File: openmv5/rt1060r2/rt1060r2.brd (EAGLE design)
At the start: 35.6 x 44.5 mm, 239 parts, among them CN1 S2B-PH-K-S(LF)(SN), IC1 LM66200DRLR, IC10 TCR2LF33,LM_CT, IC2 AP61300Z6-7, IC3 IS42S16160G-6BL, IC4 ATECC608B-MAHDA-T, IC5 IS25LP064D-JKLE-TR, IC7 MXC4005XC, IC8 MIMXRT1052DVL6B, IC9 KSZ8081RNDCA-TR, J1 USB4105-GF-A, J2 DNP, J3 DNP, J4 DF12-36-DS, J5 USD-1040310811, J6 DNP, J7 DNP, J8 3221-10-0300-00, M1 9774030151R, M2 9774030151R, Q1 2N7002KW_R1_00001, Q2 2N7002KW_R1_00001, Q3 2N7002KW_R1_00001, Q4 2N7002KW_R1_00001, Q5 2N7002KW_R1_00001, Q6 DMG2301L-7, Q7 2N7002KW_R1_00001, U2 BQ24075RGTR, U3 LBEE5KL1DX-883, Y1 SC32S-7PF20PPM, Y2 XRCGB24M000F3M00R0, Y3 ECS-327MVATX-3-CN-TR3

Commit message: Update R2 board per all feedback so far
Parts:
- removed C111: 0.1uF, 0402:0402
- removed IC10: TCR2LF33,LM_CT, TCR2LF33_LM_CT:TCR2LF33LMCT
- removed L9: MAKK2016T2R2M, MAKK2016T2R2M:INDC2016X100N
- removed U3: LBEE5KL1DX-883, LBEE5KL1DX-TEMP:XCVR_LBEE5KL1DX-TEMP
- added C24: 0.22uF, rcl:C0201
- added C25: 4.7uF, 0402:0402
- added D11, D12, D13, D14: CPDQT5V0HE-HF, CPDQT5V0HE-HF:CPDQT5V0HEHF
- added D15: RB521S30T5G, RB521S30T5G:SODFL1608X70N
- added IC6: ATECC608B-MAHDA-T, ATECC608B-MAHDA-T:SON50P300X200X60-9N
- added J9: DNP, 2337019-1:23370191
- added L3: 100, 0402:0402
- added R60, R61, R63: 10K, 0402:0402
- added R62: 2.2M, 0402:0402
- added TP1, TP2: TPTP10R, testpad:TP10R
- added U1: BQ24075RGTR, BQ24075RGTR:QFN50P300X300X100-17N
- C1: value 4.7uF -> 1nF; device sfe:0402-CAP -> 0402:0402
- C10, C40, C65, C81: value 4.7uF -> 22uF; device sfe:0402-CAP -> SparkFun-Capacitors:0805
- C101, C2, C23, C27, C3, C35, C39, C4, C41, C42, C44, C5, C57, C72, C8, C9, C92: device sfe:0402-CAP -> 0402:0402
- C103, C13, C28, C31, C38, C43, C48, C59, C62, C66, C98: value 0.22uF -> 4.7uF; device rcl:C0201 -> 0402:0402
- C104, C12, C17, C21, C60, C64, C67, C83, C90, C91, C93, C95: value 4.7uF -> 0.22uF; device sfe:0402-CAP -> rcl:C0201
- C107: value 0.22uF -> 18pF
- C108: value 4.7uF -> 18pF; device sfe:0402-CAP -> rcl:C0201
- C11, C15, C19, C34, C45: value 0.22uF -> 22uF; device rcl:C0201 -> SparkFun-Capacitors:0805
- C110: value 1nF -> 4.7uF; device sfe:0402-CAP -> 0402:0402
- C14, C61, C73, C85, C96: value 22uF -> 0.22uF; device SparkFun-Capacitors:0805 -> rcl:C0201
- C18, C37, C58, C6, C7: value 22uF -> 4.7uF; device SparkFun-Capacitors:0805 -> 0402:0402
- C20: value 1uF -> 0.22uF; device 0402:0402 -> rcl:C0201
- C22, C74: value 0.1uF -> 22uF; device 0402:0402 -> SparkFun-Capacitors:0805
- C29: value 22uF -> 1uF; device SparkFun-Capacitors:0805 -> 0402:0402
- C30, C33, C46: value 4.7uF -> 0.1uF; device sfe:0402-CAP -> 0402:0402
- C36, C82, C84: value 0.1uF -> 4.7uF
- C47, C50, C54, C55, C56: value 0.22uF -> 0.1uF; device rcl:C0201 -> 0402:0402
- C51: value 22uF -> 0.1uF; device SparkFun-Capacitors:0805 -> 0402:0402
- C52: value 4.7uF -> GRM0335C1H1R5BA01D; device sfe:0402-CAP -> GRM0335C1H1R5BA01D:CAPC0603X33N
- C53: value 0.22uF -> DNP; device rcl:C0201 -> GRM0335C1H1R5BA01D:CAPC0603X33N
- C75, C76, C89: value 0.1uF -> 0.22uF; device 0402:0402 -> rcl:C0201
- C77: value GRM0335C1H1R5BA01D -> 4.7uF; device GRM0335C1H1R5BA01D:CAPC0603X33N -> 0402:0402
- C78: value DNP -> 22uF; device GRM0335C1H1R5BA01D:CAPC0603X33N -> SparkFun-Capacitors:0805
- C79: value 18pF -> 4.7uF; device rcl:C0201 -> 0402:0402
- C80: value 18pF -> 0.22uF
- D3: value UHD1110-FKA-CL1A13R3Q1BBQFMF3 -> RB521S30T5G; device UHD1110-FKA-CL1A13R3Q1BBQFMF3:LED_UHD1110-FKA-CL1A13R3Q1BBQFMF3 -> RB521S30T5G:SODFL1608X70N
- D4: value CPDQT5V0HE-HF -> RB521S30T5G; device CPDQT5V0HE-HF:CPDQT5V0HEHF -> RB521S30T5G:SODFL1608X70N
- D5: value CPDQT5V0HE-HF -> UHD1110-FKA-CL1A13R3Q1BBQFMF3; device CPDQT5V0HE-HF:CPDQT5V0HEHF -> UHD1110-FKA-CL1A13R3Q1BBQFMF3:LED_UHD1110-FKA-CL1A13R3Q1BBQFMF3
- IC2: value AP61300Z6-7 -> TCR2LF33,LM_CT; device AP61300Z6-7:SOTFL50P162X60-6N -> TCR2LF33_LM_CT:TCR2LF33LMCT
- IC3: value IS42S16160G-6BL -> AP61300Z6-7; device IS42S16160G-6BL:BGA54C80P9X9_800X800X120 -> AP61300Z6-7:SOTFL50P162X60-6N
- IC4: value ATECC608B-MAHDA-T -> IS42S16160G-6BL; device ATECC608B-MAHDA-T:SON50P300X200X60-9N -> IS42S16160G-6BL:BGA54C80P9X9_800X800X120
- IC5: value IS25LP064D-JKLE-TR -> IS25LP128F-JKLE-TR
- IC8: value MIMXRT1052DVL6B -> KSZ8081RNDCA-TR; device MIMXRT1052DVL6B:BGA196C65P14X14_1000X1000X143 -> KSZ8081RNDCA-TR:QFN50P400X400X90-25N
- IC9: value KSZ8081RNDCA-TR -> MIMXRT1052DVL6B; device KSZ8081RNDCA-TR:QFN50P400X400X90-25N -> MIMXRT1052DVL6B:BGA196C65P14X14_1000X1000X143
- J2: value DNP -> USD-1040310811; device SparkFun-Connectors:1X08 -> 1040310811:1040310811
- J3: value DNP -> DF12-36-DS; device SparkFun-Connectors:1X08 -> DF12-36-DS:DF12-36-DS
- J4: value DF12-36-DS -> DNP; device DF12-36-DS:DF12-36-DS -> SparkFun-Connectors:1X08
- J5: value USD-1040310811 -> DNP; device 1040310811:1040310811 -> SparkFun-Connectors:1X08
- J7: device 2337019-1:23370191 -> SparkFun-Connectors:1X08
- L4, L8: device sfe:C0402 -> 0402:0402
- L5: value MAKK2016T4R7M -> 3.9NH; device MAKK2016T4R7M:INDC2016X100N -> SparkFun-Coils:0402
- L6: value 100 -> MAKK2016T2R2M; device sfe:C0402 -> MAKK2016T2R2M:INDC2016X100N
- L7: value 3.9NH -> MAKK2016T4R7M; device SparkFun-Coils:0402 -> MAKK2016T4R7M:INDC2016X100N
- Q1: value 2N7002KW_R1_00001 -> DMG2301L-7; device 2N7002KW_R1_00001:SOT65P210X110-3N -> DMG2301L-7:SOT96P240X110-3N
- Q6: value DMG2301L-7 -> 2N7002KW_R1_00001; device DMG2301L-7:SOT96P240X110-3N -> 2N7002KW_R1_00001:SOT65P210X110-3N
- R1, R5: value 1K -> 5.1K; device sfe:0402-RES -> 0402:0402
- R10: value 1.1K -> 8.2K; device sfe:0402-RES -> 0402:0402
- R11: value 46.4K -> 100K; device sfe:0402-RES -> 0402:0402
- R12: value 8.2K -> 100K; device sfe:0402-RES -> 0402:0402
- R13, R18, R34, R36, R4: device sfe:0402-RES -> 0402:0402
- R15: value 2.7K -> 200K; device sfe:0402-RES -> 0402:0402
- R16: value 2.7K -> 100K; device sfe:0402-RES -> 0402:0402
- R17: value 2.7K -> 44.2K; device sfe:0402-RES -> 0402:0402
- R19, R35: value 220 -> 100K; device sfe:0402-RES -> 0402:0402
- R2: value 200K -> 5.1K; device sfe:0402-RES -> 0402:0402
- R20: value 220 -> 1K; device sfe:0402-RES -> 0402:0402
- R21: value 220 -> 10K; device sfe:0402-RES -> 0402:0402
- R22: value 100K -> 5.1K; device sfe:0402-RES -> 0402:0402
- R23, R24, R25: value 100K -> 10K; device sfe:0402-RES -> 0402:0402
- R26: value 1K -> 2.7K; device sfe:0402-RES -> 0402:0402
- R27: value 10K -> 2.7K; device sfe:0402-RES -> 0402:0402
- R28: value 100K -> 2.7K; device sfe:0402-RES -> 0402:0402
- R29, R33, R37: value 10K -> 100K; device sfe:0402-RES -> 0402:0402
- R3: value 100K -> 1M; device sfe:0402-RES -> 0402:0402
- R30, R31: value 4.7K -> 100K; device sfe:0402-RES -> 0402:0402
- R32: value 30K -> 100K; device sfe:0402-RES -> 0402:0402
- R38: value 6.49K -> 10K; device sfe:0402-RES -> 0402:0402
- R39: value 1K -> 100K; device sfe:0402-RES -> 0402:0402
- R40: value 2.2M -> 10K; device sfe:0402-RES -> 0402:0402
- R41: value 1M -> 4.7K; device sfe:0402-RES -> 0402:0402
- R42: value 10K -> 4.7K; device sfe:0402-RES -> 0402:0402
- R45, R46: value 100K -> DNP
- R48: value 100K -> 220
- R49, R51: value 100K -> 1K
- R50: value 100K -> 6.49K
- R52, R53: value 100K -> 10K
- R56, R57, R58: value 10K -> 100K
- R59: value 100K -> 30K
- R6, R7: value 5.1K -> 10K; device sfe:0402-RES -> 0402:0402
- R8: value 44.2K -> 1.1K; device sfe:0402-RES -> 0402:0402
- R9: value 10K -> 46.4K; device sfe:0402-RES -> 0402:0402
- U2: value BQ24075RGTR -> LBEE5KL1DX-883; device BQ24075RGTR:QFN50P300X300X100-17N -> LBEE5KL1DX-TEMP:XCVR_LBEE5KL1DX-TEMP
- Y1: value SC32S-7PF20PPM -> ECS-327MVATX-3-CN-TR3; device ABS07-32.768KHZ-7-T:XTAL_ABS07-32.768KHZ-7-T -> ECS-327MVATX-3-CN-TR3:ECS327MVATX3CNTR3
- Y3: value ECS-327MVATX-3-CN-TR3 -> SC32S-7PF20PPM; device ECS-327MVATX-3-CN-TR3:ECS327MVATX3CNTR3 -> ABS07-32.768KHZ-7-T:XTAL_ABS07-32.768KHZ-7-T
- moved J2 45.9 mm to (34.9, 33.1), flipped to the bottom, turned to 270 degrees
- moved J5 44.1 mm to (4.14, 1.60), flipped to the top, turned to 90 degrees
- moved J4 42.3 mm to (1.60, 1.60), turned to 90 degrees
- moved U$2 41.4 mm to (5.20, 35.2), flipped to the top
- moved J3 41.4 mm to (17.8, 40.6), turned to 0 degrees
- moved Q6 38.0 mm to (21.5, 39.9), turned to 180 degrees
- moved R41 36.9 mm to (11.5, 40.7)
- moved J7 35.5 mm to (34.0, 1.60)
- moved R46 35.4 mm to (28.0, 8.70)
- moved Q4 34.2 mm to (8.40, 8.30), turned to 0 degrees
- moved L4 33.2 mm to (7.20, 13.3), turned to 90 degrees
- moved Q5 32.4 mm to (12.0, 8.30), turned to 180 degrees
- moved R45 32.0 mm to (25.9, 7.00), turned to 90 degrees
- moved R38 31.0 mm to (24.6, 38.1)
- moved R15 30.7 mm to (17.4, 6.20), flipped to the top, turned to 0 degrees
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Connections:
- removed net SBL_BOOT: R42.2, S1.2, S1.3, S1.4
- new net JTAG_TDI_INT_UNUSED: J8.8, R45.2
- new net JTAG_TRSTB_INT_UNUSED: J8.9, R46.2
- new net PMIC_STBY_REQ: C110.2, D15.1, IC9.L7, R63.1
- new net SBL: D13.1, J6.2, R43.2
- new net SNVS_BAT: D4.2, TP1.TP
- new net SWITCH: D15.2, R61.1, R63.2, S1.2, S1.3, S1.4
- new net VDD_SNVS_CPU: C86.1, D3.1, D4.1, IC9.M9
- net ANT: now also C52.1, J9.1, L5.2, U2.41; no longer C77.1, J7.1, L7.2, U3.41
- net BAT: now also C5.2, U1.2, U1.3; no longer C8.2, U2.2, U2.3
- net BT_D_WAKE: now also IC9.L5, U2.39; no longer IC8.L5, U3.39
- net BT_H_WAKE: now also IC9.H14, R53.1, U2.38; no longer IC8.H14, R44.1, U3.38
- net BT_REG_ON: now also IC9.F13, R44.1, U2.14; no longer IC8.F13, R37.1, U3.14
- net BT_UART_CTS: now also IC9.L12, U2.5; no longer IC8.L12, U3.5
- net BT_UART_RTS: now also IC9.K12, U2.4; no longer IC8.K12, U3.4
- net BT_UART_RX: now also IC9.C9, U2.3; no longer IC8.C9, U3.3
- net BT_UART_TX: now also IC9.B9, U2.2; no longer IC8.B9, U3.2
- net CC1: now also R1.1; no longer R6.1
- net CC2: now also R2.1; no longer R7.1
- net CHG: now also R5.1, U1.9; no longer R1.1, U2.9
- net DCDC_LP: now also IC9.M1, IC9.M2, L7.2; no longer IC8.M1, IC8.M2, L5.2
- net DCDC_PSWITCH: now also C96.1, IC9.K3, R59.1; no longer C62.1, IC8.K3, R32.1
- net DCMI_CLK: now also IC9.B14, J3.12; no longer IC8.B14, J4.12
- net DCMI_D0: now also IC9.J14, J3.31; no longer IC8.J14, J4.31
- net DCMI_D1: now also IC9.G12, J3.29; no longer IC8.G12, J4.29
- net DCMI_D2: now also IC9.H11, J3.35; no longer IC8.H11, J4.35
- net DCMI_D3: now also IC9.H12, J3.28; no longer IC8.H12, J4.28
- net DCMI_D4: now also IC9.J13, J3.26; no longer IC8.J13, J4.26
- net DCMI_D5: now also IC9.L13, J3.33; no longer IC8.L13, J4.33
- net DCMI_D6: now also IC9.G14, J3.24; no longer IC8.G14, J4.24
- net DCMI_D7: now also IC9.F11, J3.22, R43.1; no longer IC8.F11, J4.22, S1.1, S1.5
- net DCMI_FSIN: now also J3.23, Q7.3, R39.1; no longer J4.23, Q5.3, R28.1
- net DCMI_HSYNC: now also IC9.L10, J3.18; no longer IC8.L10, J4.18
- net DCMI_MISO: now also IC9.E7, J3.15; no longer IC8.E7, J4.15
- net DCMI_MOSI: now also IC9.E8, J3.17; no longer IC8.E8, J4.17
- net DCMI_PCLK: now also IC9.D13, J3.14; no longer IC8.D13, J4.14
- net DCMI_PWDN: now also IC9.C11, J3.25, R40.1; no longer IC8.C11, J4.25, R29.1
- net DCMI_RST: now also IC9.B11, J3.21, R38.1; no longer IC8.B11, J4.21, R27.1
- net DCMI_SCL: now also IC9.J11, J3.32, R41.1; no longer IC8.J11, J4.32, R30.1
- net DCMI_SCLK: now also IC9.D8, J3.13; no longer IC8.D8, J4.13
- net DCMI_SDA: now also IC9.K11, J3.34, R42.1; no longer IC8.K11, J4.34, R31.1
- net DCMI_SSEL: now also IC9.D7, J3.11, R37.1; no longer IC8.D7, J4.11, R24.1
- net DCMI_VSYNC: now also IC9.D14, J3.16; no longer IC8.D14, J4.16
- net EN: now also IC3.5, Q5.3, R16.1; no longer IC2.5, Q1.3, R3.1
- net ETH_INT: now also IC8.18, IC9.C10, R49.1; no longer IC8.C10, IC9.18, R36.1
- net ETH_LED: now also IC8.23, R48.1; no longer IC9.23, R35.1
- net ETH_MDC: now also IC8.11, IC9.A7; no longer IC8.A7, IC9.11
- net ETH_MDIO: now also IC8.10, IC9.C7, R51.1; no longer IC8.C7, IC9.10, R39.1
- net ETH_RST: now also C42.2, IC8.24, IC9.D10, R47.1; no longer C65.2, IC8.D10, IC9.24, R34.1
- net ETH_RXD0: now also IC8.13, IC9.E12; no longer IC8.E12, IC9.13
- net ETH_RXD1: now also IC8.12, IC9.D12; no longer IC8.D12, IC9.12
- net ETH_RXDV: now also IC8.15, IC9.C12; no longer IC8.C12, IC9.15
- net ETH_RXERR: now also IC8.17, IC9.C13; no longer IC8.C13, IC9.17
- net ETH_TXCLK: now also IC8.8, IC9.B13; no longer IC8.B13, IC9.8
- net ETH_TXD0: now also IC8.20, IC9.B12; no longer IC8.B12, IC9.20
- net ETH_TXD1: now also IC8.21, IC9.A12; no longer IC8.A12, IC9.21
- net ETH_TXEN: now also IC8.19, IC9.A13; no longer IC8.A13, IC9.19
- net ETH_VDDA_3.3: now also C43.2, C45.1, C46.1, IC8.2, L4.1; no longer C81.2, C82.1, C85.1, IC9.2, L8.1
- net ETH_VDD_1.2: now also C44.2, C47.1, IC8.1; no longer C83.2, C84.1, IC9.1
- net FB: now also IC3.1, R15.1, R17.2; no longer IC2.1, R2.1, R8.2
- net FEED: now also C53.1, L5.1; no longer C78.1, L7.1
- net GND: now also C10.2, C104.2, C108.2, C11.2, C12.1, C17.2, C19.1, C21.2, C23.2, C24.1, C25.1, C28.1, C33.2, C36.1, C37.1, C38.1, C40.2, C43.1, C46.2, C48.1, C49.2, C52.2, C59.1, C6.1, C60.2, C61.2, C62.1, C68.2, C7.1, C73.2, C74.1, C77.1, C78.1, C79.1, C85.1, C86.2, C87.2, C88.1, C89.1, C90.2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; no longer C10.1, C104.1, C108.1, C11.1, C111.2, C12.2, C17.1, C19.2, C21.1, C23.1, C28.2, C33.1, C36.2, C37.2, C38.2, C40.1, C43.2, C46.1, C48.2, C49.1, C52.1, C59.2, C6.2, C60.1, C61.1, C62.2, C68.1, C7.2, C73.1, C74.2, C77.2, C78.2, C79.2, C85.2, C86.1, C87.1, C88.2, C89.2, C90.1, C99.1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
- net ILIM: now also R8.1, U1.12; no longer R10.1, U2.12
- net INT_I2C_INT: now also IC9.D11, R28.1; no longer IC8.D11, R17.1
- net INT_I2C_SCL: now also IC6.6, IC9.C8, R26.1; no longer IC4.6, IC8.C8, R15.1
- net INT_I2C_SDA: now also IC6.5, IC9.B8, R27.1; no longer IC4.5, IC8.B8, R16.1
- net ISET: now also R10.1, U1.16; no longer R12.1, U2.16
- net JTAG_TCK: now also FL5.5, IC9.F12; no longer FL5.4, IC8.F12
- net JTAG_TCK_INT: now also FL5.8; no longer FL5.9
- net JTAG_TDI: now also FL5.3, IC9.F14; no longer FL5.2, IC8.F14
- net JTAG_TDI_INT: now also FL5.10, J6.4, R45.1; no longer FL5.11, J8.8
- net JTAG_TDO: now also FL5.4, IC9.G13; no longer FL5.3, IC8.G13
- net JTAG_TDO_INT: now also FL5.9; no longer FL5.10
- net JTAG_TMS: now also FL5.6, IC9.E14; no longer FL5.5, IC8.E14
- net JTAG_TMS_INT: now also FL5.7; no longer FL5.8
- net JTAG_TRSTB: now also FL5.1, IC9.G10; no longer FL5.6, IC8.G10
- net JTAG_TRSTB_INT: now also FL5.12, J6.3, R46.1; no longer FL5.7, J8.9
- net LED_B: now also IC9.C14, R20.1, R23.1; no longer IC8.C14, R19.1, R56.1
- net LED_B_INT: now also D5.1, R20.2; no longer D3.1, R19.2
- net LED_CHG: now also R5.2; no longer R1.2
- net LED_G: now also IC9.A10, R21.1, R24.1; no longer IC8.A10, R20.1, R57.1
- net LED_G_INT: now also D5.2, R21.2; no longer D3.2, R20.2
- net LED_PGOOD: now also R6.2; no longer R4.2
- net LED_R: now also IC9.D9, R22.1, R25.1; no longer IC8.D9, R21.1, R58.1
- net LED_R_INT: now also D5.3, R22.2; no longer D3.3, R21.2
- net LED_ST: now also R4.2; no longer R5.2
- net LPO_IN: now also U2.37, Y1.3; no longer U3.37, Y3.3
- net MDI_LED: now also J5.8, R48.2; no longer J3.8, R35.2
- net MDI_RX_N: now also IC8.3, J5.7; no longer IC9.3, J3.7
- net MDI_RX_P: now also IC8.4, J5.6; no longer IC9.4, J3.6
- net MDI_TX_N: now also IC8.5, J5.5; no longer IC9.5, J3.5
- net MDI_TX_P: now also IC8.6, J5.4; no longer IC9.6, J3.4
- net NVCC_PLL: now also C101.2, C102.1, IC9.P10; no longer C104.2, C107.1, IC8.P10
- net ONOFF: now also IC9.M6, Q4.2; no longer IC8.M6, Q3.2
- net ON_BATTERY: now also IC9.P2, Q2.2, R12.1; no longer IC8.P2, Q7.2, R59.1
- net P0_MOSI: now also FL3.1, IC9.H10; no longer FL2.1, IC8.H10
- net P0_MOSI_INT: now also FL3.12, J4.8; no longer FL2.12, J2.8
- net P10_PWM: now also Q6.3, R36.1; no longer Q4.3, R26.1
- net P10_PWM_INT: now also J7.6; no longer J6.6
- net P11_WAKEUP: now also Q3.3, R13.1; no longer Q2.3, R22.1
- net P11_WAKEUP_INT: now also J7.7; no longer J6.7
- net P12_RST_N: now also C109.1, FL5.2, IC9.M7, R60.2; no longer C63.1, FL5.1, IC8.M7, R33.2
- net P12_RST_N_EXT: now also FL5.11, J7.8; no longer FL5.12, J6.8
- net P1_MISO: now also FL3.2, IC9.M11; no longer FL2.2, IC8.M11
- net P1_MISO_INT: now also FL3.11, J4.7; no longer FL2.11, J2.7
- net P2_SCLK: now also FL3.3, IC9.M14; no longer FL2.3, IC8.M14
- net P2_SCLK_INT: now also FL3.10, J4.6; no longer FL2.10, J2.6
- net P3_NSS: now also FL3.4, IC9.G11; no longer FL2.4, IC8.G11
- net P3_NSS_INT: now also FL3.9, J4.5; no longer FL2.9, J2.5
- net P4_SCL: now also FL3.5, IC9.K14; no longer FL2.5, IC8.K14
- net P4_SCL_INT: now also FL3.8, J4.4; no longer FL2.8, J2.4
- net P5_SDA: now also FL3.6, IC9.L14; no longer FL2.6, IC8.L14
- net P5_SDA_INT: now also FL3.7, J4.3; no longer FL2.7, J2.3
- net P6_ADC: now also IC9.M12; no longer IC8.M12
- net P6_ADC_INT: now also J4.2; no longer J2.2
- net P7_PWM: now also IC9.A8; no longer IC8.A8
- net P7_PWM_INT: now also J7.3; no longer J6.3
- net P8_PWM: now also IC9.A9; no longer IC8.A9
- net P8_PWM_INT: now also J7.4; no longer J6.4
- net P9_PWM: now also IC9.A11; no longer IC8.A11
- net P9_PWM_INT: now also J7.5; no longer J6.5
- net PGOOD: now also Q2.3, R11.1, R6.1, U1.7; no longer Q7.3, R14.1, R4.1, U2.7
- net PMIC_ONOFF: now also D11.1, J5.3, Q4.3, R14.1; no longer D8.1, J3.3, Q3.3, R23.1
- net PMIC_ON_REQ: now also IC9.K7, Q5.2; no longer IC8.K7, Q1.2
- net PWM_FSIN: now also IC9.M5, Q6.2, Q7.2, R35.1; no longer IC8.M5, Q4.2, Q5.2, R25.1
- net P_FLASH_CE: now also IC9.L3, R19.2; no longer IC8.L3, R13.2
- net P_FLASH_IO0: now also IC9.P3; no longer IC8.P3
- net P_FLASH_IO1: now also IC9.N4; no longer IC8.N4
- net P_FLASH_IO2: now also IC9.P4; no longer IC8.P4
- net P_FLASH_IO3: now also IC9.P5; no longer IC8.P5
- net P_FLASH_SCK: now also IC9.L4; no longer IC8.L4
- net RAW: now also C10.1, C7.2, C8.2, D9.1, IC2.1, IC3.3, J5.2, R11.2, R13.2, R16.2, U1.10, U1.11, U1.5; no longer C1.2, C10.2, C6.1, D5.1, IC10.1, IC10.3, J3.2, R22.2, R23.2, R3.2, U2.10, U2.11, U2.5
- net REXT: now also IC8.9, R50.1; no longer IC9.9, R38.1
- net RTC_XTALI: now also C108.1, IC9.N9, Y3.2; no longer C80.1, IC8.N9, Y1.2
- net RTC_XTALO: now also C107.1, IC9.P9, Y3.1; no longer C79.1, IC8.P9, Y1.1
- net SDRAM_A0: now also IC4.H7, IC9.C2; no longer IC3.H7, IC8.C2
- net SDRAM_A1: now also IC4.H8, IC9.G1; no longer IC3.H8, IC8.G1
- net SDRAM_A10: now also IC4.H9, IC9.G2; no longer IC3.H9, IC8.G2
- net SDRAM_A11: now also IC4.G2, IC9.B4; no longer IC3.G2, IC8.B4
- net SDRAM_A12: now also IC4.G1, IC9.A3; no longer IC3.G1, IC8.A3
- net SDRAM_A2: now also IC4.J8, IC9.G3; no longer IC3.J8, IC8.G3
- net SDRAM_A3: now also IC4.J7, IC9.H1; no longer IC3.J7, IC8.H1
- net SDRAM_A4: now also IC4.J3, IC9.A6; no longer IC3.J3, IC8.A6
- net SDRAM_A5: now also IC4.J2, IC9.B6; no longer IC3.J2, IC8.B6
- net SDRAM_A6: now also IC4.H3, IC9.B1; no longer IC3.H3, IC8.B1
- net SDRAM_A7: now also IC4.H2, IC9.A5; no longer IC3.H2, IC8.A5
- net SDRAM_A8: now also IC4.H1, IC9.A4; no longer IC3.H1, IC8.A4
- net SDRAM_A9: now also IC4.G3, IC9.B2; no longer IC3.G3, IC8.B2
- net SDRAM_BA0: now also IC4.G7, IC9.C1; no longer IC3.G7, IC8.C1
- net SDRAM_BA1: now also IC4.G8, IC9.F1; no longer IC3.G8, IC8.F1
- net SDRAM_CAS: now also IC4.F7, IC9.D3; no longer IC3.F7, IC8.D3
- net SDRAM_CKE: now also IC4.F3, IC9.A2; no longer IC3.F3, IC8.A2
- net SDRAM_CLK: now also IC4.F2, IC9.B3; no longer IC3.F2, IC8.B3
- net SDRAM_CS: now also IC4.G9, IC9.E1; no longer IC3.G9, IC8.E1
- net SDRAM_DQ0: now also IC4.A8, IC9.E3; no longer IC3.A8, IC8.E3
- net SDRAM_DQ1: now also IC4.B9, IC9.F3; no longer IC3.B9, IC8.F3
- net SDRAM_DQ10: now also IC4.D1, IC9.D5; no longer IC3.D1, IC8.D5
- net SDRAM_DQ11: now also IC4.C2, IC9.C4; no longer IC3.C2, IC8.C4
- net SDRAM_DQ12: now also IC4.C1, IC9.D4; no longer IC3.C1, IC8.D4
- net SDRAM_DQ13: now also IC4.B2, IC9.E5; no longer IC3.B2, IC8.E5
- net SDRAM_DQ14: now also IC4.B1, IC9.C3; no longer IC3.B1, IC8.C3
- net SDRAM_DQ15: now also IC4.A2, IC9.E4; no longer IC3.A2, IC8.E4
- net SDRAM_DQ2: now also IC4.B8, IC9.F4; no longer IC3.B8, IC8.F4
- net SDRAM_DQ3: now also IC4.C9, IC9.G4; no longer IC3.C9, IC8.G4
- net SDRAM_DQ4: now also IC4.C8, IC9.F2; no longer IC3.C8, IC8.F2
- net SDRAM_DQ5: now also IC4.D9, IC9.G5; no longer IC3.D9, IC8.G5
- net SDRAM_DQ6: now also IC4.D8, IC9.H5; no longer IC3.D8, IC8.H5
- net SDRAM_DQ7: now also IC4.E9, IC9.H4; no longer IC3.E9, IC8.H4
- net SDRAM_DQ8: now also IC4.E1, IC9.C6; no longer IC3.E1, IC8.C6
- net SDRAM_DQ9: now also IC4.D2, IC9.C5; no longer IC3.D2, IC8.C5
- net SDRAM_DQMH: now also IC4.F1, IC9.D6; no longer IC3.F1, IC8.D6
- net SDRAM_DQML: now also IC4.E8, IC9.H3; no longer IC3.E8, IC8.H3
- net SDRAM_RAS: now also IC4.F8, IC9.D2; no longer IC3.F8, IC8.D2
- net SDRAM_WE: now also IC4.F9, IC9.D1; no longer IC3.F9, IC8.D1
- net SD_CD: now also D7.1, IC9.L11, J2.CD$1, R29.1; no longer D9.1, IC8.L11, J5.CD$1, R50.1
- net SD_CLK: now also FL2.4, IC9.J3; no longer FL3.4, IC8.J3
- net SD_CLK_INT: now also FL2.9, J2.P$5; no longer FL3.9, J5.P$5
- net SD_CMD: now also FL2.3, IC9.J4, R32.1; no longer FL3.3, IC8.J4, R53.1
- net SD_CMD_INT: now also FL2.10, J2.P$3; no longer FL3.10, J5.P$3
- net SD_DAT0: now also FL2.5, IC9.J1, R31.1; no longer FL3.5, IC8.J1, R52.1
- net SD_DAT0_INT: now also FL2.8, J2.P$7; no longer FL3.8, J5.P$7
- net SD_DAT1: now also FL2.6, IC9.K1, R30.1; no longer FL3.6, IC8.K1, R51.1
- net SD_DAT1_INT: now also FL2.7, J2.P$8; no longer FL3.7, J5.P$8
- net SD_DAT2: now also FL2.1, IC9.H2, R34.1; no longer FL3.1, IC8.H2, R55.1
- net SD_DAT2_INT: now also FL2.12, J2.P$1; no longer FL3.12, J5.P$1
- net SD_DAT3: now also FL2.2, IC9.J2, R33.1; no longer FL3.2, IC8.J2, R54.1
- net SD_DAT3_INT: now also FL2.11, J2.P$2; no longer FL3.11, J5.P$2
- net SHELL_GND: now also C1.2, R3.1; no longer C110.2, R41.1
- net SR_VLX: now also L6.1, U2.34; no longer L9.1, U3.34
- net ST: now also R4.1; no longer R5.1
- net SW: now also IC3.4; no longer IC2.4
- net TMR: now also R9.1, U1.14; no longer R11.1, U2.14
- net TS: now also R7.1, U1.1; no longer R9.1, U2.1
- net USB_D_N: now also IC9.M8; no longer IC8.M8
- net USB_D_P: now also IC9.L8; no longer IC8.L8
- net VBUS: now also C2.2, C90.1, C92.2, IC9.N6; no longer C3.2, C88.1, C95.2, IC8.N6
- net VCC: now also C103.2, C104.1, C11.1, C12.2, C17.1, C19.2, C21.1, C23.1, C24.2, C25.2, C28.2, C33.1, C34.1, C36.2, C37.2, C38.2, C48.2, C49.1, C51.1, C59.2, C69.1, C70.1, C71.1, C77.2, C78.2, C82.1, C83.2, C84.1, C85.2, C88.2, C95.2, D12.1, D14.1, D5.4, D8.1, IC3.6, IC4.A7, IC4.A9, IC4.B3, IC4.C7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; no longer C108.2, C109.1, C11.2, C111.1, C12.1, C17.2, C19.1, C21.2, C23.2, C28.1, C33.2, C36.1, C37.1, C40.2, C41.2, C42.2, C43.1, C44.2, C53.1, C54.1, C57.2, C64.1, C68.2, C7.1, C86.2, C89.1, C90.2, C92.2, C93.2, C96.1, C99.2, D10.1, D3.4, D4.1, IC2.6, IC3.A7, IC3.A9, IC3.B3, IC3.C7, IC3.D3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
- net VCC_SOC: now also C60.1, C61.1, C62.2, C63.1, C64.1, C65.2, C68.1, C89.2, C91.2, C93.2, IC9.F6, IC9.F7, IC9.F8, IC9.F9, IC9.G6, IC9.G9, IC9.H6, IC9.H9, IC9.J5, IC9.J9, L7.1; no longer C103.2, C34.1, C38.1, C45.1, C46.2, C47.1, C48.1, C49.2, C87.2, C98.2, IC8.F6, IC8.F7, IC8.F8, IC8.F9, IC8.G6, IC8.G9, IC8.H6, IC8.H9, IC8.J5, IC8.J9, L5.1
- net VDDA: now also C40.1, C41.2, J3.4, L3.1; no longer C51.1, C52.2, J4.4, L4.1
- net VDDA_ADC_3P3: now also C72.2, C73.1, C74.2, IC9.N14, L8.1; no longer C59.1, C60.2, C61.2, IC8.N14, L6.1
- net VDD_HIGH_CAP: now also C98.2, C99.1, IC9.P8; no longer C101.2, C102.1, IC8.P8
- net VDD_SNVS: now also C9.2, D3.2, IC2.5, Q4.1, Q5.1, R61.2; no longer C2.2, C69.1, IC10.5, IC8.M9, Q1.1, Q2.1
- net VDD_SNVS_CAP: now also C87.1, IC9.M10; no longer C70.1, IC8.M10
- net VDD_USB_CAP: now also C79.2, C80.1, C81.2, IC9.K8; no longer C71.1, C72.2, C73.2, IC8.K8
- net VIN: now also D10.1, J7.2, Q1.3; no longer D7.1, J6.2, Q6.3
- net VIN_INT: now also C4.2, Q1.2; no longer C5.2, Q6.2
- net VIN_LDO: now also C54.1, C57.2, L6.2, U2.31; no longer C74.1, C91.2, L9.2, U3.31
- net V_BATT: now also C3.2, C6.2, U1.13; no longer C4.2, C9.2, U2.13
- net WAKEUP: now also IC9.L6, Q3.2; no longer IC8.L6, Q2.2
- net WIFI_CLK: now also IC9.M13, U2.20; no longer IC8.M13, U3.20
- net WIFI_CMD: now also IC9.H13, R58.1, U2.22; no longer IC8.H13, R49.1, U3.22
- net WIFI_D0: now also IC9.M4, R57.1, U2.24; no longer IC8.M4, R48.1, U3.24
- net WIFI_D1: now also IC9.M3, R56.1, U2.26; no longer IC8.M3, R47.1, U3.26
- net WIFI_D2: now also IC9.J12, R55.1, U2.23; no longer IC8.J12, R46.1, U3.23
- net WIFI_D3: now also IC9.K10, R54.1, U2.25; no longer IC8.K10, R45.1, U3.25
- net WL_H_WAKE: now also IC9.E11, R52.1, U2.27; no longer IC8.E11, R43.1, U3.27
- net WL_REG_ON: now also IC9.E10, U2.28; no longer IC8.E10, U3.28
- net XTALI: now also IC9.P11, R62.1; no longer IC8.P11, R40.1
- net XTALO: now also IC9.N11; no longer IC8.N11
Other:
- board text added: "5.16.23"
- board text added: "OpenMV RT R2"
- board text added: "RES RES RES RES P14 P13 SBL 3.3V"
- board text added: "USER"
- board text added: "WKE"
- board text removed: "3.21.23"
- board text removed: "IR"
- board text removed: "OpenMV RT R1"
- board text removed: "W"
- board text removed: "WAKE"

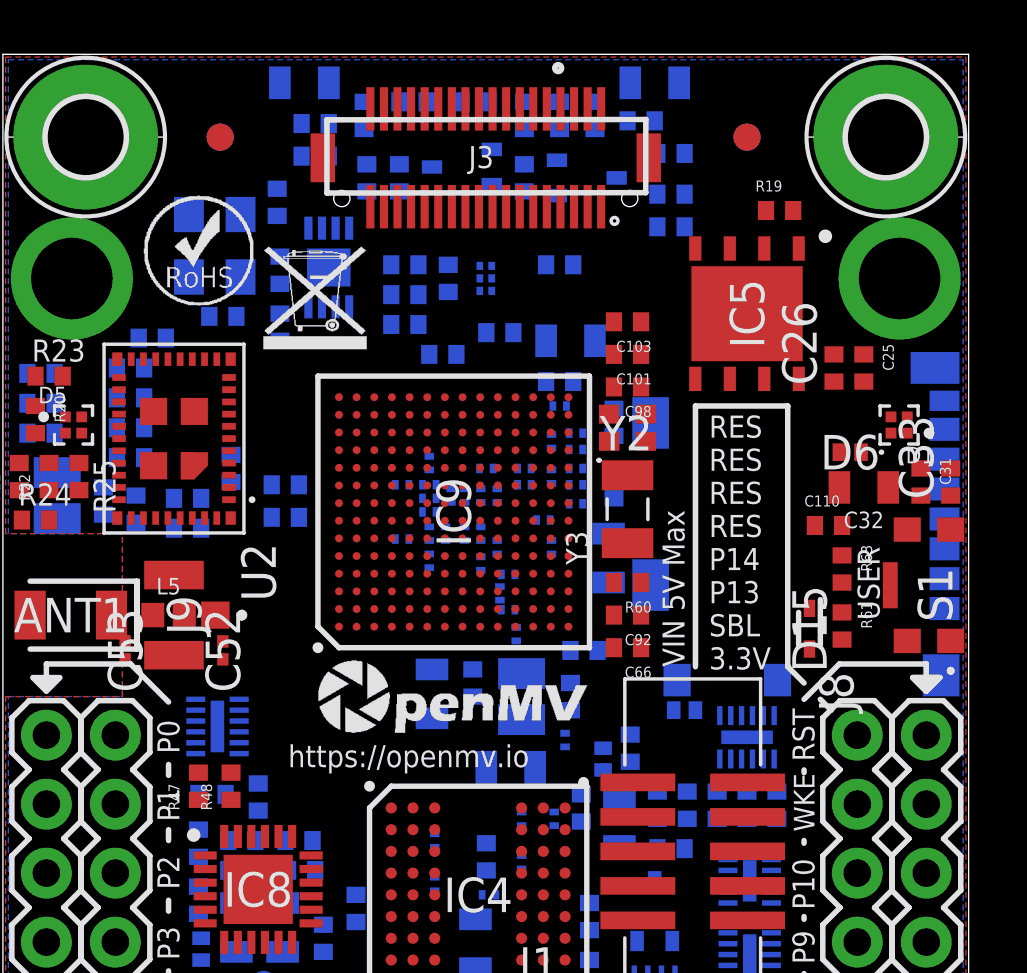
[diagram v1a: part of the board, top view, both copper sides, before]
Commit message: Evaluate power off issues and fix
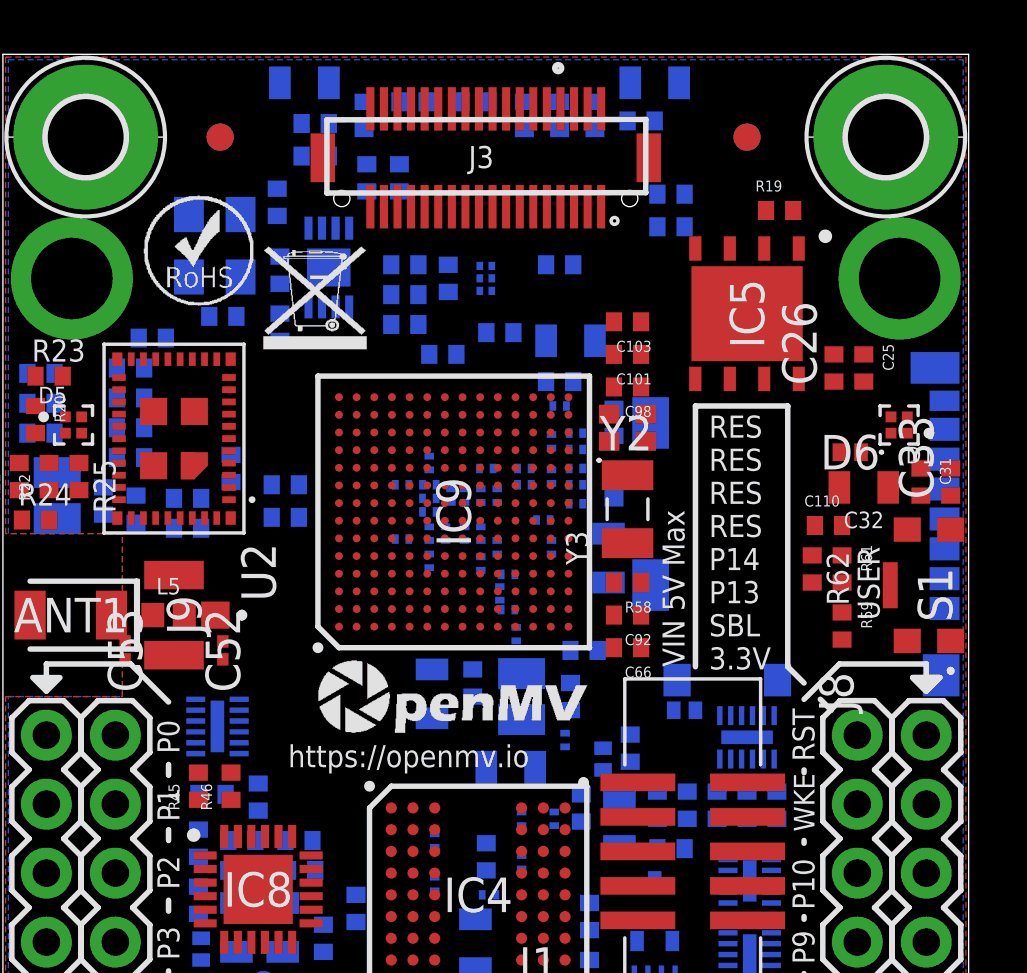
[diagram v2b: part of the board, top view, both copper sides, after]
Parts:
- removed D15: RB521S30T5G, RB521S30T5G:SODFL1608X70N
- removed Q6, Q7: 2N7002KW_R1_00001, 2N7002KW_R1_00001:SOT65P210X110-3N
- removed R63: 10K, 0402:0402
- R36, R51: value 1K -> 10K
- R39: value 100K -> 4.7K
- R40: value 10K -> 4.7K
- R41, R42: value 4.7K -> 10K
- R43, R44: value 10K -> DNP
- R45: value DNP -> 100K
- R46: value DNP -> 220
- R47: value 100K -> 1K
- R48: value 220 -> 6.49K
- R50: value 6.49K -> 10K
- R52, R53: value 10K -> 100K
- R57: value 100K -> 30K
- R59: value 30K -> 10K
- R60: value 10K -> 2.2M
- R62: value 2.2M -> 10K
- moved R44 32.8 mm to (28.0, 8.70), turned to 0 degrees
- moved R43 28.1 mm to (25.9, 7.00), turned to 90 degrees
- moved R46 21.5 mm to (8.40, 17.5), flipped to the top, turned to 90 degrees
- moved R45 21.4 mm to (7.20, 17.5), flipped to the top
- moved R50 20.6 mm to (4.70, 29.6)
- moved R58 19.7 mm to (23.0, 25.0), flipped to the top
- moved R57 19.7 mm to (21.4, 22.5)
- moved R51 17.6 mm to (8.40, 29.2)
- moved R38 11.3 mm to (13.4, 39.9), turned to 90 degrees
- moved R37 10.0 mm to (14.6, 39.9), turned to 90 degrees
- moved R59 9.54 mm to (30.9, 23.4), flipped to the top, turned to 270 degrees
- moved R62 9.08 mm to (29.8, 25.5), flipped to the top, turned to 270 degrees
- moved R41 8.68 mm to (16.2, 33.4)
- moved R48 7.95 mm to (11.3, 10.1), flipped to the bottom, turned to 180 degrees
- moved R42 7.87 mm to (8.10, 34.8)
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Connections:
- removed net P10_PWM: FL4.5, Q6.3, R36.1
- removed net PWM_FSIN: IC9.M5, Q6.2, Q7.2, R35.1
- new net SWITCH_OUT: C110.2, R61.1, R62.2
- net BT_H_WAKE: now also R51.1; no longer R53.1
- net BT_REG_ON: now also R42.1; no longer R44.1
- net DCDC_PSWITCH: now also R57.1; no longer R59.1
- net DCMI_D7: now also R41.1; no longer R43.1
- net DCMI_FSIN: now also FL4.5, IC9.M5, R37.1; no longer Q7.3, R39.1
- net DCMI_PWDN: now also R38.1; no longer R40.1
- net DCMI_RST: now also R36.1; no longer R38.1
- net DCMI_SCL: now also R39.1; no longer R41.1
- net DCMI_SDA: now also R40.1; no longer R42.1
- net DCMI_SSEL: now also R35.1; no longer R37.1
- net ETH_INT: now also R47.1; no longer R49.1
- net ETH_LED: now also R46.1; no longer R48.1
- net ETH_MDIO: now also R49.1; no longer R51.1
- net ETH_RST: now also R45.1; no longer R47.1
- net GND: now also R36.2, R42.2, R48.2, R60.2; no longer R38.2, R44.2, R50.2, R62.2
- net JTAG_TDI_INT: now also R43.1; no longer R45.1
- net JTAG_TDI_INT_UNUSED: now also R43.2; no longer R45.2
- net JTAG_TRSTB_INT: now also R44.1; no longer R46.1
- net JTAG_TRSTB_INT_UNUSED: now also R44.2; no longer R46.2
- net MDI_LED: now also R46.2; no longer R48.2
- net P12_RST_N: now also R58.2; no longer R60.2
- net PMIC_STBY_REQ: now also R62.1; no longer C110.2, D15.1, R63.1
- net REXT: now also R48.1; no longer R50.1
- net SBL: now also R41.2; no longer R43.2
- net SWITCH: now also R59.1, R61.2; no longer D15.2, R61.1, R63.2
- net VCC: now also R38.2, R45.2, R50.2, R58.1; no longer Q6.1, Q7.1, R36.2, R41.2, R42.2, R58.2, R60.1
- net VDD_SNVS: no longer R61.2
- net WIFI_CMD: now also R56.1; no longer R58.1
- net WIFI_D0: now also R55.1; no longer R57.1
- net WIFI_D1: now also R54.1; no longer R56.1
- net WIFI_D2: now also R53.1; no longer R55.1
- net WIFI_D3: now also R52.1; no longer R54.1
- net WL_H_WAKE: now also R50.1; no longer R52.1
- net XTALI: now also R60.1; no longer R62.1

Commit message: Fx leakage issue
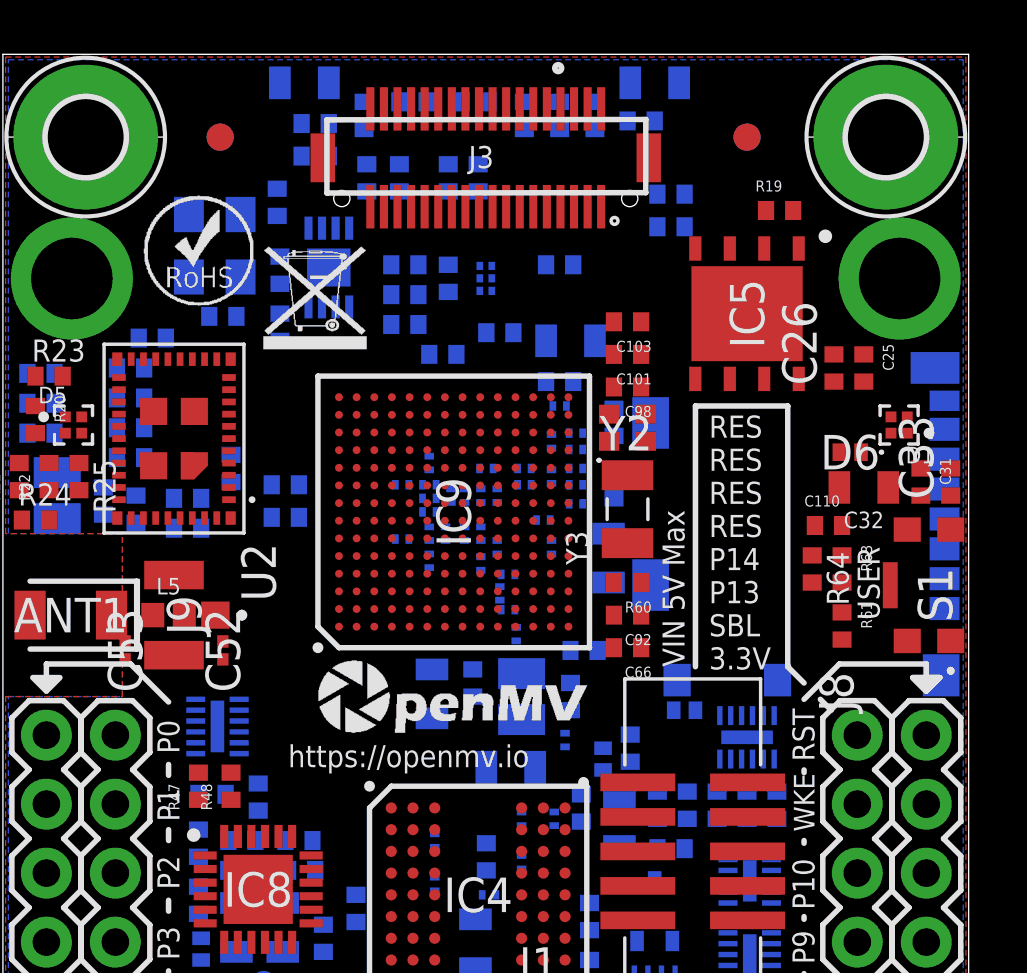
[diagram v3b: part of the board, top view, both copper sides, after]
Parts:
- added R63: 10K, 0402:0402
- added R64: 100K, 0402:0402
- R37, R52, R53: value 100K -> 10K
- R38: value 10K -> 4.7K
- R40: value 4.7K -> 100K
- R41, R42, R51: value 10K -> 1K
- R43, R44: value DNP -> 10K
- R45: value 100K -> DNP
- R46: value 220 -> DNP
- R47: value 1K -> 100K
- R48: value 6.49K -> 220
- R50: value 10K -> 6.49K
- R57: value 30K -> 100K
- R59: value 10K -> 30K
- R60: value 2.2M -> 100K
- R62: value 10K -> 2.2M
- moved R44 32.8 mm to (8.10, 34.8), turned to 180 degrees
- moved R43 28.1 mm to (16.2, 33.4), turned to 180 degrees
- moved R46 21.5 mm to (28.0, 8.70), flipped to the bottom, turned to 0 degrees
- moved R45 21.4 mm to (25.9, 7.00), flipped to the bottom
- moved R50 20.6 mm to (11.3, 10.1)
- moved R58 19.7 mm to (5.50, 34.0), flipped to the bottom
- moved R57 19.7 mm to (4.70, 32.9)
- moved R51 17.6 mm to (11.8, 11.9)
- moved R42 10.7 mm to (17.5, 39.9), turned to 270 degrees
- moved R59 9.54 mm to (21.4, 22.5), flipped to the bottom, turned to 180 degrees
- moved R62 9.08 mm to (22.5, 30.9), flipped to the bottom, turned to 90 degrees
- moved R48 7.95 mm to (8.40, 17.5), flipped to the top, turned to 90 degrees
- moved R53 7.83 mm to (8.40, 29.2), turned to 90 degrees
- moved R41 6.50 mm to (16.4, 39.9), turned to 270 degrees
- moved R60 5.92 mm to (23.0, 25.0), flipped to the top, turned to 180 degrees
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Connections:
- new net P10_PWM: FL4.5, R42.1
- new net PWM_FSIN: IC9.M5, R40.1, R41.2, R42.2
- net BT_H_WAKE: now also R53.1; no longer R51.1
- net BT_REG_ON: now also R44.1; no longer R42.1
- net DCDC_PSWITCH: now also R59.1; no longer R57.1
- net DCMI_D7: now also R43.1; no longer R41.1
- net DCMI_FSIN: now also R41.1; no longer FL4.5, IC9.M5, R37.1
- net DCMI_PWDN: now also R37.1; no longer R38.1
- net DCMI_SCL: now also R38.1; no longer R39.1
- net DCMI_SDA: now also R39.1; no longer R40.1
- net ETH_INT: now also R49.1; no longer R47.1
- net ETH_LED: now also R48.1; no longer R46.1
- net ETH_MDIO: now also R51.1; no longer R49.1
- net ETH_RST: now also R47.1; no longer R45.1
- net GND: now also R44.2, R50.2, R62.2; no longer R42.2, R48.2, R60.2
- net JTAG_TDI_INT: now also R45.1; no longer R43.1
- net JTAG_TDI_INT_UNUSED: now also R45.2; no longer R43.2
- net JTAG_TRSTB_INT: now also R46.1; no longer R44.1
- net JTAG_TRSTB_INT_UNUSED: now also R46.2; no longer R44.2
- net MDI_LED: now also R48.2; no longer R46.2
- net P12_RST_N: now also R60.2; no longer R58.2
- net PMIC_STBY_REQ: now also R64.1; no longer R62.1
- net RAW: now also D1.4
- net REXT: now also R50.1; no longer R48.1
- net SBL: now also R43.2; no longer R41.2
- net SWITCH: now also R61.1, R63.2; no longer R59.1, R61.2
- net SWITCH_OUT: now also R63.1, R64.2; no longer R61.1, R62.2
- net VCC: now also R58.2, R60.1, R61.2; no longer R45.2, R50.2, R58.1
- net V_BATT: no longer D1.4
- net WIFI_CMD: now also R58.1; no longer R56.1
- net WIFI_D0: now also R57.1; no longer R55.1
- net WIFI_D1: now also R56.1; no longer R54.1
- net WIFI_D2: now also R55.1; no longer R53.1
- net WIFI_D3: now also R54.1; no longer R52.1
- net WL_H_WAKE: now also R52.1; no longer R50.1
- net XTALI: now also R62.1; no longer R60.1

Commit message: Fix processor name
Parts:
- IC9: value MIMXRT1052DVL6B -> MIMXRT106FCVL5B
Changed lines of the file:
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@@
 <attribute name="VALUE" x="2.843" y="27.8205" size="0.4064" layer="27" rot="R90"/>
 </element>
-<element name="IC9" library="MIMXRT1052DVL6B" package="BGA196C65P14X14_1000X1000X143" value="MIMXRT1052DVL6B" x="16.6" y="27.6" smashed="yes" rot="R90">
-<attribute name="DESCRIPTION" value="Processors - Application Specialized MIMXRT1052DVL6B/LFBGA196///STANDARD MARKING * TRAY" x="16.6" y="27.6" size="1.778" layer="27" rot="R90" display="off"/>
+<element name="IC9" library="MIMXRT1052DVL6B" package="BGA196C65P14X14_1000X1000X143" value="MIMXRT106FCVL5B" x="16.6" y="27.6" smashed="yes" rot="R90">
+<attribute name="DESCRIPTION" value="Processors - Application Specialized MIMXRT1062DVL6B/LFBGA196///STANDARD MARKING * TRAY" x="16.6" y="27.6" size="1.778" layer="27" rot="R90" display="off"/>
 <attribute name="HEIGHT" value="1.43mm" x="16.6" y="27.6" size="1.778" layer="27" rot="R90" display="off"/>
 <attribute name="MANUFACTURER_NAME" value="NXP" x="16.6" y="27.6" size="1.778" layer="27" rot="R90" display="off"/>
-<attribute name="MANUFACTURER_PART_NUMBER" value="MIMXRT1052DVL6B" x="16.6" y="27.6" size="1.778" layer="27" rot="R90" display="off"/>
-<attribute name="MOUSER_PART_NUMBER" value="771-MIMXRT1052DVL6B" x="16.6" y="27.6" size="1.778" layer="27" rot="R90" display="off"/>
-<attribute name="MOUSER_PRICE-STOCK" value="https://www.mouser.co.uk/ProductDetail/NXP-Semiconductors/MIMXRT1052DVL6B?qs=r5DSvlrkXmLhWvqckzJtSg%3D%3D" x="16.6" y="27.6" size="1.778" layer="27" rot="R90" display="off"/>
-<attribute name="MPN" value="MIMXRT1052DVL6B" x="16.6" y="27.6" size="1.778" layer="27" rot="R90" display="off"/>
+<attribute name="MANUFACTURER_PART_NUMBER" value="MIMXRT1062DVL6B" x="16.6" y="27.6" size="1.778" layer="27" rot="R90" display="off"/>
+<attribute name="MOUSER_PART_NUMBER" value="771-MIMXRT1062DVL6B" x="16.6" y="27.6" size="1.778" layer="27" rot="R90" display="off"/>
+<attribute name="MOUSER_PRICE-STOCK" value="https://www.mouser.co.uk/ProductDetail/NXP-Semiconductors/MIMXRT1062DVL6B" x="16.6" y="27.6" size="1.778" layer="27" rot="R90" display="off"/>
+<attribute name="MPN" value="MIMXRT106FCVL5B" x="16.6" y="27.6" size="1.778" layer="27" rot="R90" display="off"/>
 <attribute name="NAME" x="16.6" y="27.6" size="1.27" layer="25" rot="R90" align="center"/>
 <attribute name="VALUE" x="16.6" y="27.6" size="1.27" layer="27" rot="R90" align="center"/>

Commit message: Fix label issues
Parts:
- C29: value 1uF -> 0.1uF
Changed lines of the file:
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@@
 <attribute name="VALUE" x="12" y="36.6" size="1.27" layer="28" rot="MR270" align="center"/>
 </element>
-<element name="C29" library="0402" package="0402" value="1uF" x="10.2" y="34.4" smashed="yes" rot="MR270">
+<element name="C29" library="0402" package="0402" value="0.1uF" x="10.2" y="34.4" smashed="yes" rot="MR270">
 <attribute name="MPN" value="C0402C104Z4VAC" x="10.2" y="34.4" size="1.778" layer="28" rot="MR270" display="off"/>
 <attribute name="NAME" x="9.565" y="35.035" size="1.27" layer="26" rot="MR270"/>
